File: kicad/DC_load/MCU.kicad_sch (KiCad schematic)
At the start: 101 parts, among them J1 BNC, J6 USB_B, J8 Conn_01x05_Socket, J9 Conn_01x04_Socket, Q1 MMBT5401, SW1 RotaryEncoder_Switch, SW2 RotaryEncoder_Switch, SW3 SW_Push, SW8 SW_Push, U1 FSA3157P6X, U10 FSA3157P6X, U11 FSA3157P6X, U12 FSA3157P6X, U14 AMS1117-3.3, U15 74HC14D653, U16 93LCxxB, U17 CH340C, U18 TL431DBZ, U2 Screen, U8 STM32F103C8Tx, U9 Front plate

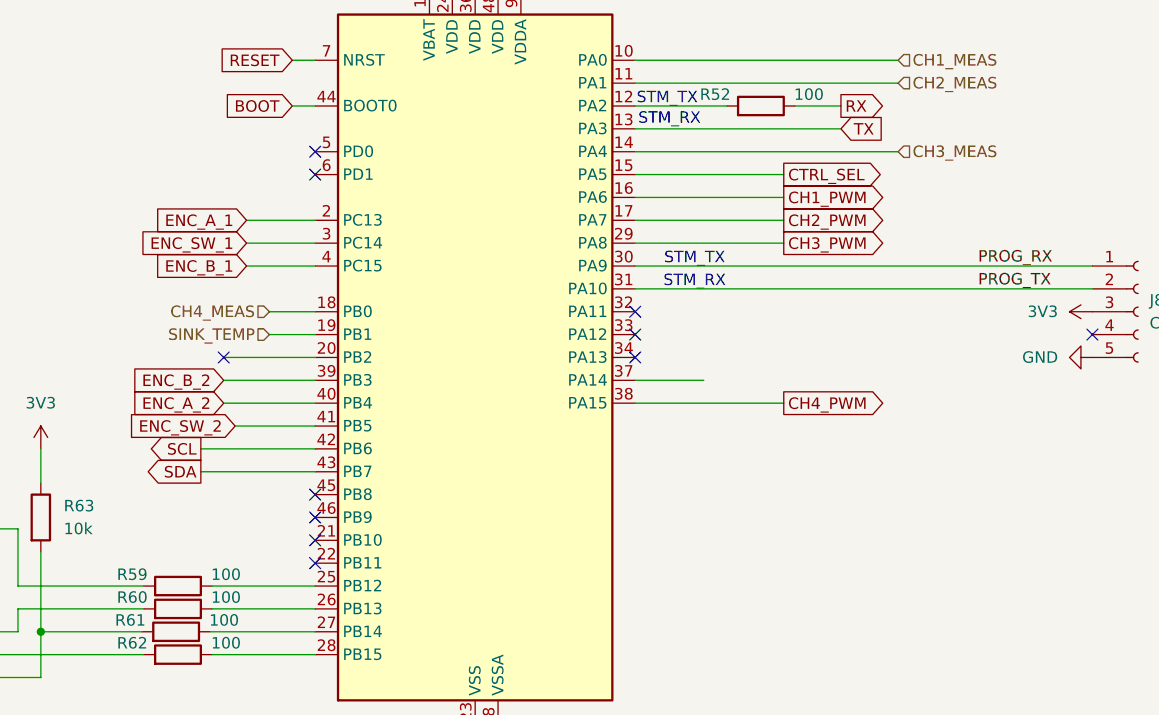
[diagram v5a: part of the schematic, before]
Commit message: Added voltage sense
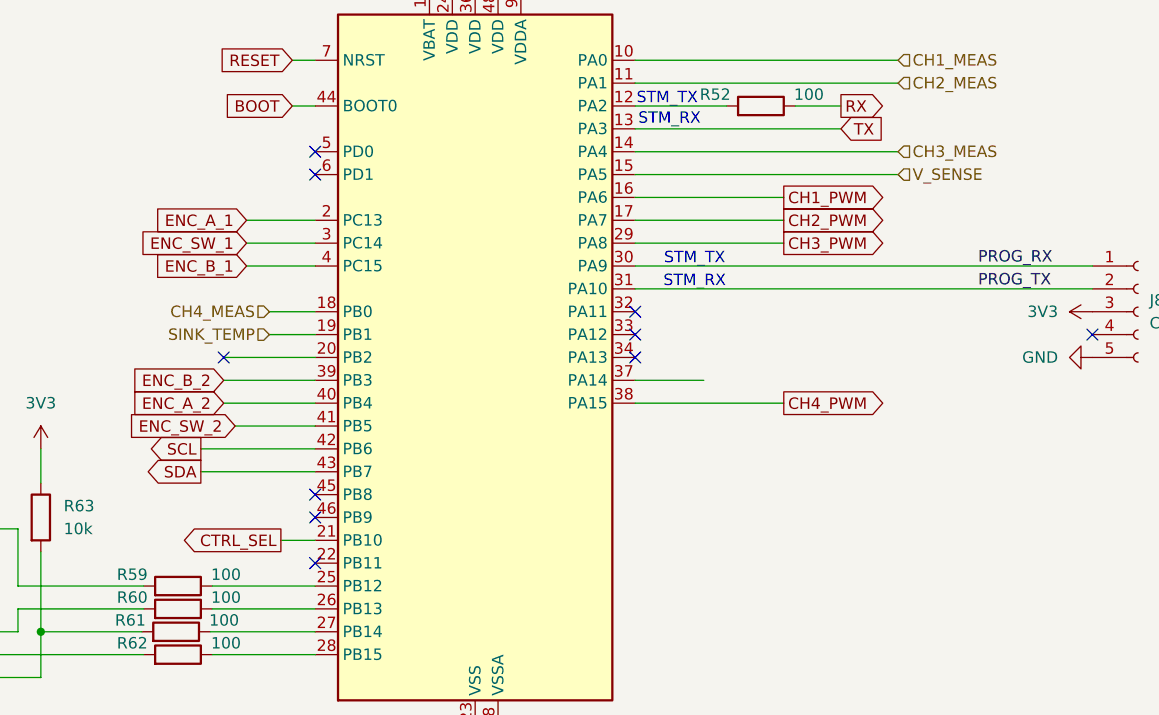
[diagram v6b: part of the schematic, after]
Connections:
- net CTRL_SEL: now also U8.21 (PB10); no longer U8.15 (PA5)
- new net V_SENSE: U8.15 (PA5)
- no-connect marks 20 -> 19
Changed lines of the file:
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@@
 	)
 	(no_connect
-		(at 292.1 210.82)
-	)
-	(no_connect
 		(at 281.94 190.5)
 	)
@@
 	(wire
 		(pts
+			(xy 288.29 210.82) (xy 292.1 210.82)
+		)
+		(stroke
+			(width 0)
+			(type default)
+		)
+	)
+	(wire
+		(pts
 			(xy 356.87 157.48) (xy 327.66 157.48)
 		)
@@
 	(wire
 		(pts
-			(xy 344.17 170.18) (xy 327.66 170.18)
+			(xy 327.66 170.18) (xy 356.87 170.18)
 		)
 		(stroke
@@
 		)
 	)
-	(global_label "CH1_CONTROL"
+	(global_label "CTRL_SEL"
 		(shape output)
-		(at 129.54 30.48 0)
+		(at 288.29 210.82 180)
 		(fields_autoplaced yes)
 		(effects
@@
 				(size 1.27 1.27)
 			)
-			(justify left)
+			(justify right)
 		)
 		(property "Intersheetrefs" "${INTERSHEET_REFS}"
-			(at 145.83 30.48 0)
+			(at 276.4149 210.82 0)
 			(effects
 				(font
 					(size 1.27 1.27)
 				)
-				(justify left)
+				(justify right)
 				(hide yes)
 			)
 		)
 	)
-	(global_label "CH1_PWM"
+	(global_label "CH1_CONTROL"
 		(shape output)
-		(at 344.17 172.72 0)
+		(at 129.54 30.48 0)
 		(fields_autoplaced yes)
 		(effects
@@
 		)
 		(property "Intersheetrefs" "${INTERSHEET_REFS}"
-			(at 356.1056 172.72 0)
+			(at 145.83 30.48 0)
 			(effects
 				(font
@@
 		)
 	)
-	(global_label "CTRL_SEL"
+	(global_label "CH1_PWM"
 		(shape output)
-		(at 344.17 170.18 0)
+		(at 344.17 172.72 0)
 		(fields_autoplaced yes)
 		(effects
@@
 		)
 		(property "Intersheetrefs" "${INTERSHEET_REFS}"
-			(at 356.0451 170.18 0)
+			(at 356.1056 172.72 0)
 			(effects
 				(font
@@
 		(effects
 			(font
+				(size 1.27 1.27)
+			)
+			(justify left)
+		)
+	)
+	(hierarchical_label "V_SENSE"
+		(shape input)
+		(at 356.87 170.18 0)
+		(effects
+			(font

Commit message: DC fan boost converter added.
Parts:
- added C54, C56, C57: 10u, Resistor_SMD:R_0805_2012Metric_Pad1.20x1.40mm_HandSolder, symbol Device:C
- added C55: 100n, Capacitor_SMD:C_0603_1608Metric_Pad1.08x0.95mm_HandSolder, symbol Device:C
- added D5: 1N5819WS, Diode_SMD:D_SOD-323, symbol Diode:1N5819WS
- added J7: Conn_01x04_Socket, Connector_PinSocket_2.54mm:PinSocket_1x04_P2.54mm_Vertical, symbol Connector:Conn_01x04_Socket
- added L4: 4.7u, Inductor_SMD:L_Bourns_SRN6045TA, symbol solar_push_pull_sym_lib:SRN6045HA-4R7Y
- added Q13: AO3400A, Package_TO_SOT_SMD:SOT-23, symbol Transistor_FET:AO3400A
- J8: value Conn_01x05_Socket -> FT232 programming port
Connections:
- net 5V: now also C56.2, C57.2, L4.1
- net GND: now also C54.1, C55.2, C56.1, C57.1, J7.1 (Pin_1), Q13.2 (S); no longer U15.3, U15.5
- net at U15.4: now also U15.6, Q13.1 (G)
- net FAN_BOOST: now reaches U8.32 (PA11)
- net FAN_BOOST: now also U15.3, U15.5
- new net: C54.2, C55.1, D5.1 (K), J7.2 (Pin_2)
- new net: D5.2 (A), L4.2, Q13.3 (D)
- no-connect marks 19 -> 18
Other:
- note added: "12 V fan 100 mArms"
- note added: "MCU buttons"
- moved on the sheet: C21, C22, C23, C24, C25, C26, C27, C28, C30, C31, C32, C33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

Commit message: Done.
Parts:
- removed J7: Conn_01x04_Socket, Connector_PinSocket_2.54mm:PinSocket_1x04_P2.54mm_Vertical, symbol Connector:Conn_01x04_Socket
- added C58, C59, C60, C61, C62, C63: 10u, Capacitor_SMD:C_0603_1608Metric_Pad1.08x0.95mm_HandSolder, symbol Device:C
- added J10: DC fan connector, Connector_PinHeader_2.54mm:PinHeader_1x04_P2.54mm_Vertical, symbol Connector:Conn_01x04_Pin
- added R64, R65: 10k, Resistor_SMD:R_0603_1608Metric_Pad0.98x0.95mm_HandSolder, symbol Device:R
- added R66: 49.9k, Resistor_SMD:R_0603_1608Metric_Pad0.98x0.95mm_HandSolder, symbol Device:R
- added TP1, TP2, TP3, TP4, TP5, TP6, TP7: TestPoint, TestPoint:TestPoint_Pad_D2.0mm, symbol Connector:TestPoint
- C54, C56, C57: footprint Resistor_SMD:R_0805_2012Metric_Pad1.20x1.40mm_HandSolder -> Capacitor_SMD:C_0603_1608Metric_Pad1.08x0.95mm_HandSolder; LCSC C15850 -> C96446; Voltage 25V -> (none)
- L4: footprint Inductor_SMD:L_Bourns_SRN6045TA -> DC_load:L_Bourns_SRN6045TA
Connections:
- net 3V3: now also R64.1, TP3.1
- net 5V: now also C56.1, C57.1, C58.1, C59.1, C60.1, TP1.1; no longer C56.2, C57.2
- net CH2_PWM: now also U8.41 (PB5); no longer U8.17 (PA7)
- net ENC_SW_2: now also U8.45 (PB8); no longer U8.41 (PB5)
- net GND: now also C54.2, C56.2, C57.2, C58.2, C59.2, C60.2, C61.2, C62.2, C63.2, J10.1 (Pin_1), R65.2, TP4.1, TP5.1, TP7.1; no longer C54.1, C56.1, C57.1
- net VREF: now also TP2.1
- net FAN_OUT: now reaches C55.1, D5.1 (K)
- net FAN_OUT: now also C54.1, C61.1, C62.1, C63.1, J10.2 (Pin_2), R66.1, TP6.1; no longer C54.2
- net FAN_DRAIN: now reaches D5.2 (A), L4.2, Q13.3 (D)
- new net FAN_VOLT: R65.1, R66.2, U8.17 (PA7)
- new net TACH: J10.3 (Pin_3), R64.2
- no-connect marks 18 -> 16
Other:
- moved on the sheet: C30, C31, C55, D5, L4, Q13, U14, U15B, U15C
